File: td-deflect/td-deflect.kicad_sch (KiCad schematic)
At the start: 77 parts, among them J10 Conn_01x02_Male, J11 Conn_01x02_Male, J12 Conn_01x06_Male, J3 Conn_01x02_Male, Q1 BSC082N10LSG, Q10 IPD50R380CE, Q11 IPD50R380CE, Q2 C2M0045170D, Q3 BSC082N10LSG, Q4 BCP56, Q5 BCP53, Q6 BD139, Q7 BD140, Q8 IPD50R380CE, Q9 IPD50R380CE, T1 CST1-125LC, U1 MCP1416, U10 MIC4427, U5 TL082, U6 IRS2005S, U7 LTC6090, U8 INA181, U9 MIC4427

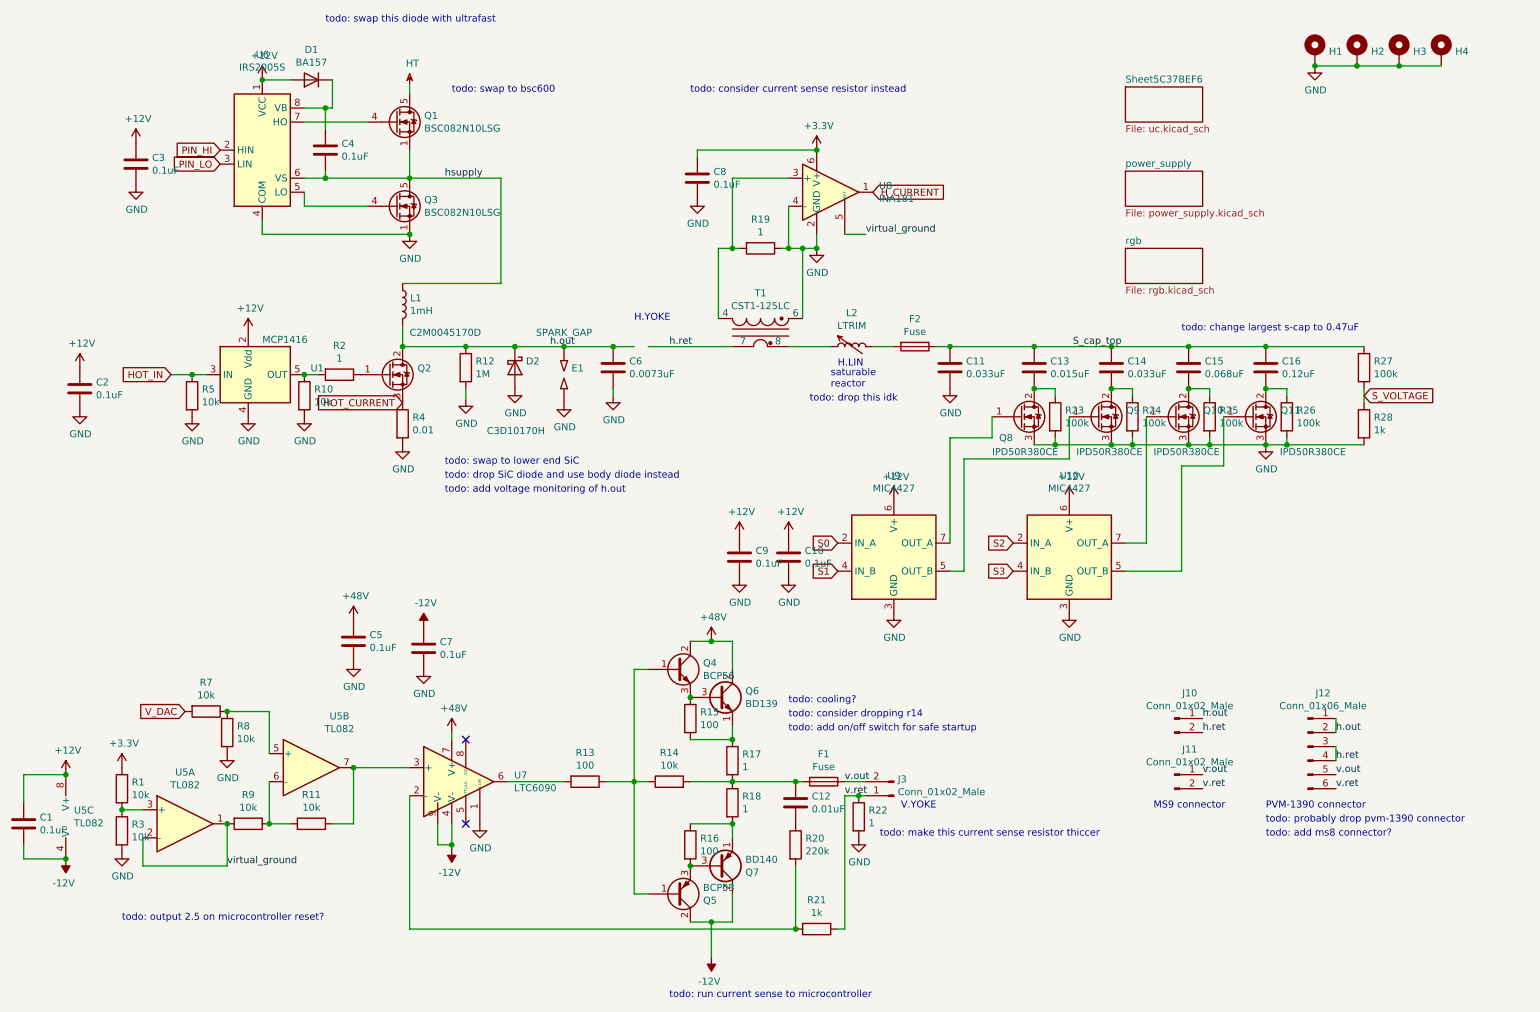
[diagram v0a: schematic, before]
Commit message: Implemented some of the ToDos
Replaced current transformer for horizontal current measurement with a shunt  Replaced R22 with a bigger resistor (0.5W)  Replaced SiC-MOSFETs with smaller and cheaper alternatives  Removed HOT_CURRENT measurement  Replaced Q1 & Q3 with BSC600
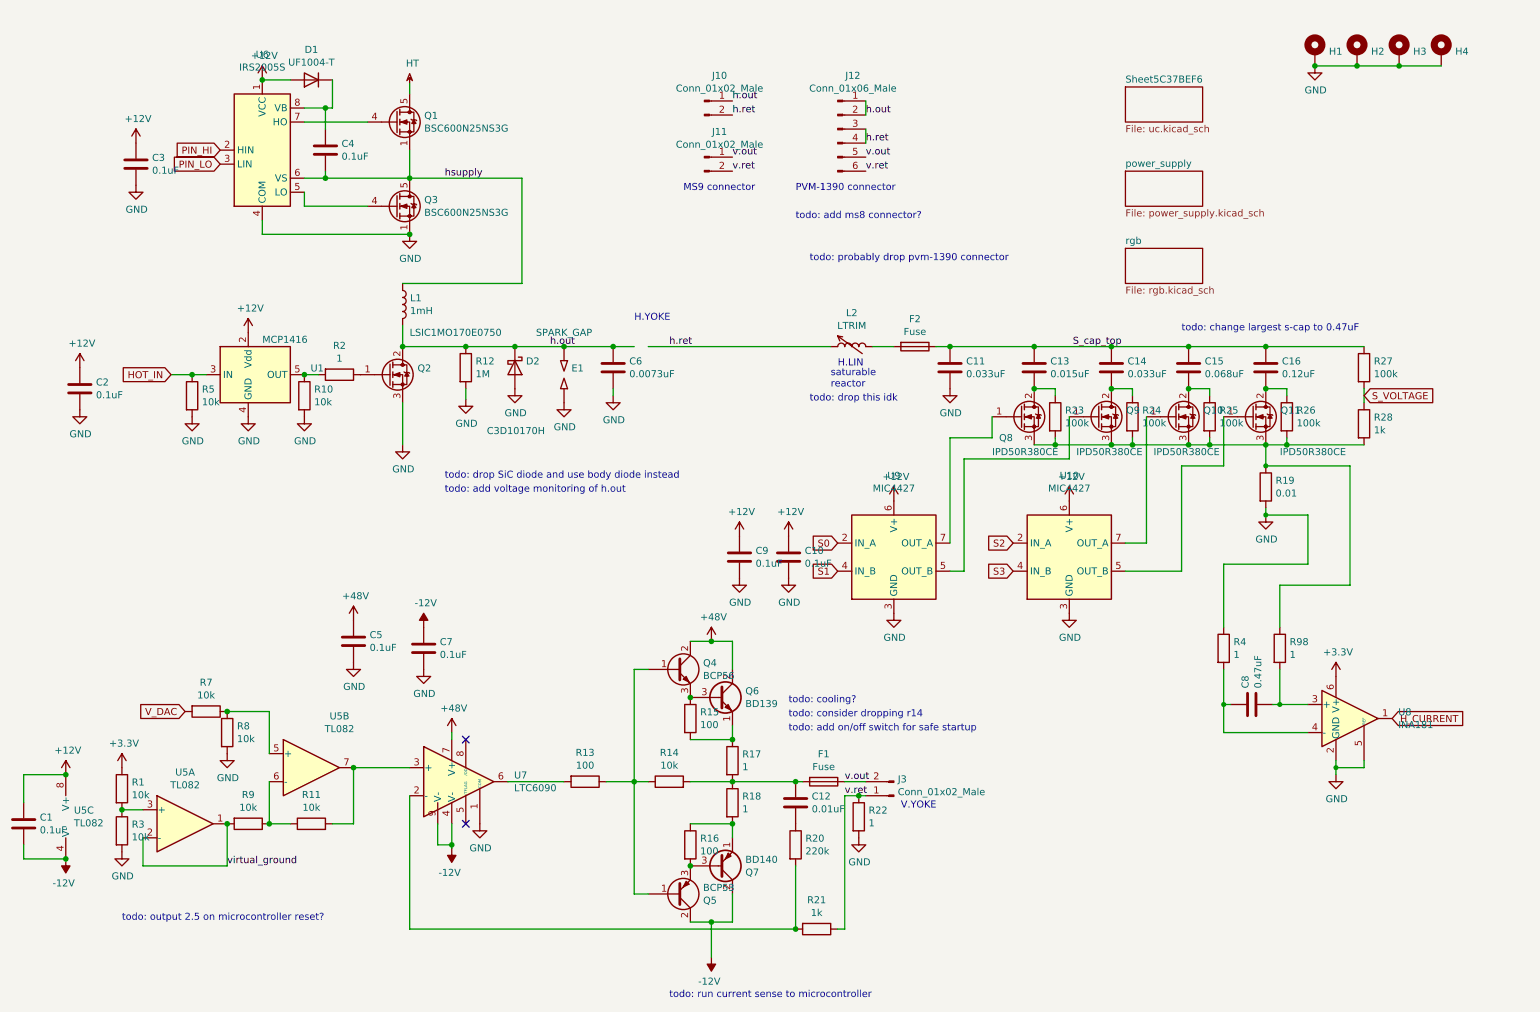
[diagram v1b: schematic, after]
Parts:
- removed T1: CST1-125LC, Transformer_SMD:Transformer_Coilcraft_CST1, symbol Transformer:CST1
- added R98: 1, Resistor_SMD:R_0805_2012Metric_Pad1.15x1.40mm_HandSolder, symbol Device:R
- C8: value 0.1uF -> 0.47uF; Digikey 1276-1099-1-ND -> 399-C0805C474K5RAC7800CT-ND; Voltage 10V -> (none)
- D1: value BA157 -> UF1004-T; Digikey BA157-E3/54GICT-ND -> UF1004DICT-ND
- Q1, Q3: value BSC082N10LSG -> BSC600N25NS3G; Digikey BSC082N10LSGATMA1CT-ND -> BSC600N25NS3GATMA1CT-ND
- Q2: value C2M0045170D -> LSIC1MO170E0750; Digikey C2M0045170D-ND -> 18-LSIC1MO170E0750-ND
- R19: value 1 -> 0.01; Digikey 311-1.00CRCT-ND -> 311-0.01NUCT-ND
- R22: Digikey 311-1.00CRCT-ND -> ERJ-6DQF1R0V
- R4: value 0.01 -> 1; Digikey 311-0.01NUCT-ND -> 311-1.00CRCT-ND
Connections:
- net HOT_CURRENT is gone; now on net GND: Q2.3 (S), R4.1
- net +3V3: no longer C8.1
- net GND: now also R19.2, U8.5 (REF); no longer C8.2, Q10.3 (S), Q11.3 (S), Q8.3 (S), Q9.3 (S), R19.1, R23.2, R24.2, R25.2, R26.2, R28.2, R4.2, U8.4 (-)
- net h.ret: now also L2.1
- net virtual_ground: no longer U8.5 (REF)
- net at U8.3 (+): now also C8.2, R98.2; no longer R19.2
- new net: Q10.3 (S), Q11.3 (S), Q8.3 (S), Q9.3 (S), R19.1, R23.2, R24.2, R25.2, R26.2, R28.2, R98.1
- new net: C8.1, R4.2, U8.4 (-)
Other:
- note removed: "todo: consider current sense resistor instead"
- note removed: "todo: make this current sense resistor thiccer"
- note removed: "todo: swap this diode with ultrafast"
- note removed: "todo: swap to bsc600"
- note removed: "todo: swap to lower end SiC"
- moved on the sheet: J10, J11, J12, U8
